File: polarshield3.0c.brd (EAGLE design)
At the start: 81.1 x 66 mm, 45 parts

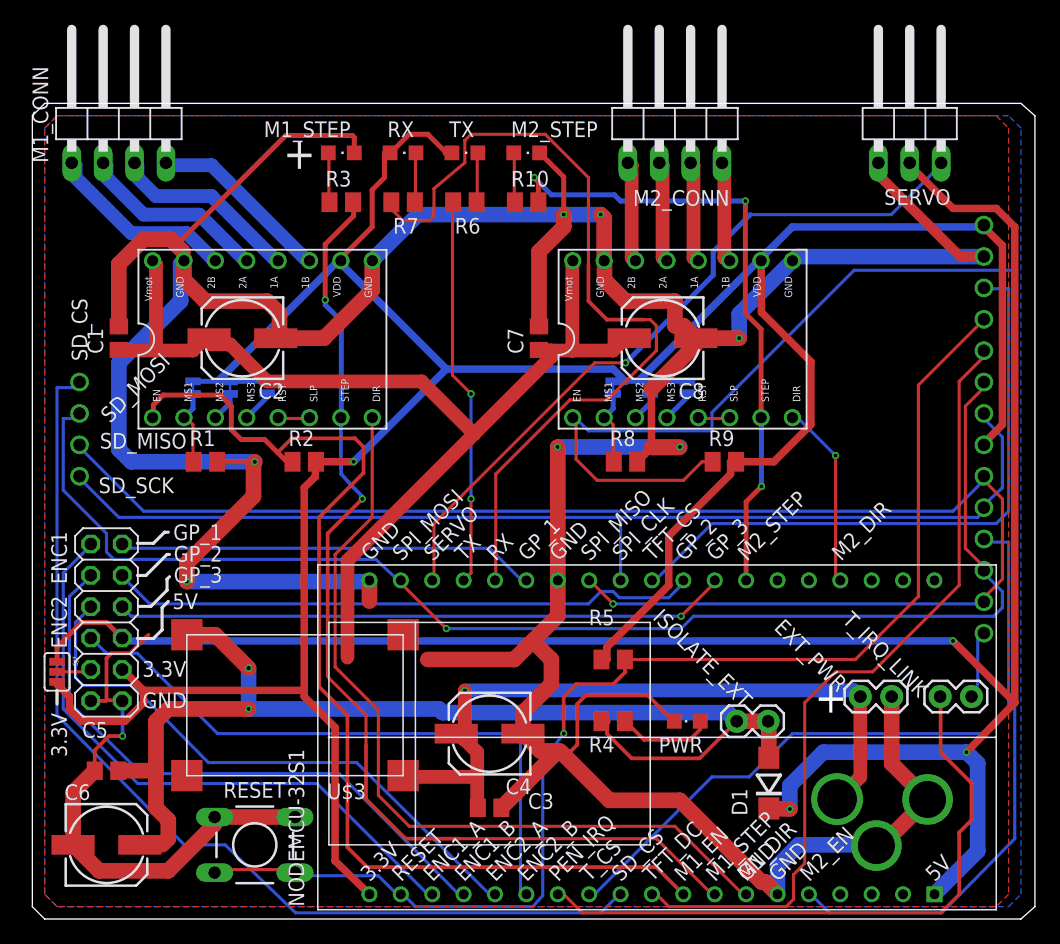
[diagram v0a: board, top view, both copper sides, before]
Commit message: Minor changes based on first board.
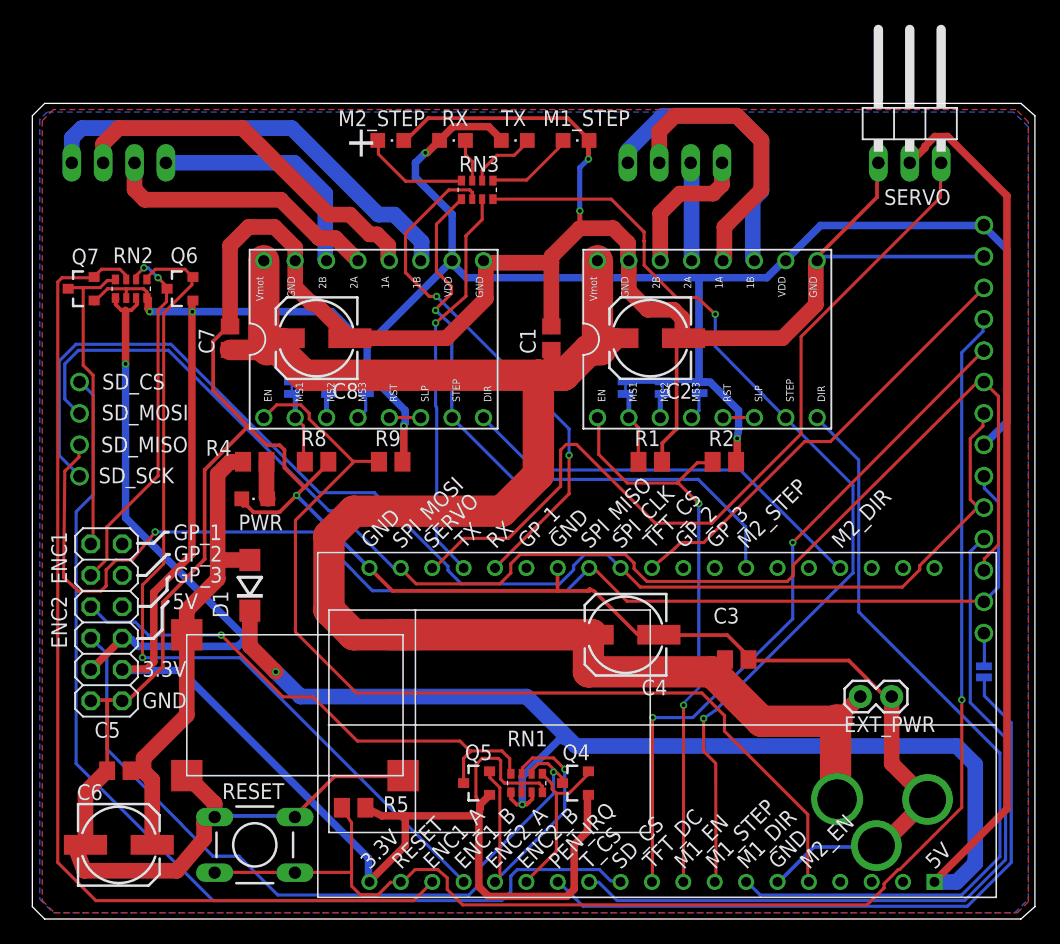
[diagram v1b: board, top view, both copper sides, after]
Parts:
- removed ISOLATE_EXT, T_IRQ_LINK: (no value), SparkFun-Connectors:1X02
- removed R10, R3, R6, R7: 1k, resistor:M0805
- removed SJ7: (no value), SparkFun-Retired:SJ_3_PASTE1&2
- added Q4, Q5, Q6, Q7: BSS138, SparkFun:SOT23-3
- added RN1, RN2: 10k, resistor-dil:EXB38V
- added RN3: 1k, resistor-dil:EXB38V
- added SJ8: T_IRQ_LINK, SparkFun-Retired:SJ_2S-NO
- moved M1_CONN 45.0 mm to (52.0, 65.0), flipped to the bottom
- moved M2_CONN 45.0 mm to (7.00, 65.0), flipped to the bottom
- moved D1 44.9 mm to (17.6, 27.0)
- moved PWR 39.4 mm to (18.0, 34.0)
- moved MOTOR_1 36.0 mm to (47.0, 52.0)
- moved R1 36.0 mm to (50.0, 37.0)
- moved R4 35.8 mm to (18.0, 37.0)
- moved C1 35.0 mm to (42.0, 47.0)
- moved SJ1 35.0 mm to (54.0, 43.0)
- moved SJ2 35.0 mm to (51.0, 43.0)
- moved SJ3 35.0 mm to (48.0, 43.0)
- moved R2 34.0 mm to (56.0, 37.0)
- moved C2 33.0 mm to (50.0, 47.0)
- moved C8 28.0 mm to (23.0, 47.0)
- moved R9 27.0 mm to (29.0, 37.0)
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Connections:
- removed net N$28: SJ7.2, SPARE_BREAKOUT.4
- new net ENC1_A_HV: Q7.3, RN2.4, SPARE_BREAKOUT.12
- new net ENC1_B_HV: Q6.3, RN2.2, SPARE_BREAKOUT.10
- new net ENC2_A_HV: Q5.3, RN1.4, SPARE_BREAKOUT.8
- new net ENC2_B_HV: Q4.3, RN1.2, SPARE_BREAKOUT.6
- new net GP_1_HV: SPARE_BREAKOUT.11
- new net GP_2_HV: SPARE_BREAKOUT.9
- new net GP_3_HV: SPARE_BREAKOUT.7
- net +3V3: now also Q4.1, Q5.1, Q6.1, Q7.1, RN1.6, RN1.8, RN2.6, RN2.8; no longer SJ7.3
- net +5V: now also RN1.5, RN1.7, RN2.5, RN2.7, SPARE_BREAKOUT.4; no longer SJ7.1
- net ENC1_A: now also Q7.2, RN2.3; no longer SPARE_BREAKOUT.12
- net ENC1_B: now also Q6.2, RN2.1; no longer SPARE_BREAKOUT.10
- net ENC2_A: now also Q5.2, RN1.3; no longer SPARE_BREAKOUT.8
- net ENC2_B: now also Q4.2, RN1.1; no longer SPARE_BREAKOUT.6
- net GP_1: no longer SPARE_BREAKOUT.11
- net GP_2: no longer SPARE_BREAKOUT.9
- net GP_3: no longer SPARE_BREAKOUT.7
- net M1_STEP: now also RN3.4; no longer R3.2
- net M2_STEP: now also RN3.1; no longer R10.2
- net N$1: now also SJ8.2; no longer T_IRQ_LINK.2
- net N$14: now also RN3.6; no longer R6.1
- net N$15: now also RN3.7; no longer R7.1
- net N$19: now also RN3.8; no longer R10.1
- net N$6: now also RN3.5; no longer R3.1
- net N$7: no longer ISOLATE_EXT.1, ISOLATE_EXT.2
- net RX: now also RN3.2; no longer R7.2
- net TX: now also RN3.3; no longer R6.2
- net T_IRQ: now also SJ8.1; no longer T_IRQ_LINK.1
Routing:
- net ENC2_B_HV: track 0.00 -> 60.6 mm, vias 0 -> 1
- net GND: track 384.7 -> 328.7 mm, vias 8 -> 3
- net N$7: track 92.3 -> 38.9 mm, vias 2 -> 0
- net GP_3: track 49.6 -> 0.00 mm, vias 1 -> 0
- net GP_2: track 47.7 -> 0.00 mm
- net ENC2_A_HV: track 0.00 -> 43.8 mm, vias 0 -> 1
- net M2_EN: track 124.2 -> 81.5 mm
- net +5V: track 169.4 -> 209.5 mm
- net M1_EN: track 87.3 -> 47.5 mm, vias 0 -> 2
- net ENC2_B: track 51.4 -> 13.7 mm
- net ENC1_A: track 50.3 -> 85.7 mm
- net GP_1: track 33.9 -> 0.00 mm
- net +3V3: track 243.2 -> 273.4 mm, vias 1 -> 5
- net ENC1_B_HV: track 0.00 -> 29.7 mm, vias 0 -> 2
- net N$23: track 8.26 -> 36.0 mm
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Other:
- board text added: "An open source art project. 2018.05.14"
- board text added: "Polarshield v3.0c"
- board text removed: "An open source art project. 2018.04.22"
- board text removed: "Polarshield v3.0"
